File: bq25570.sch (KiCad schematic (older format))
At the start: 32 parts

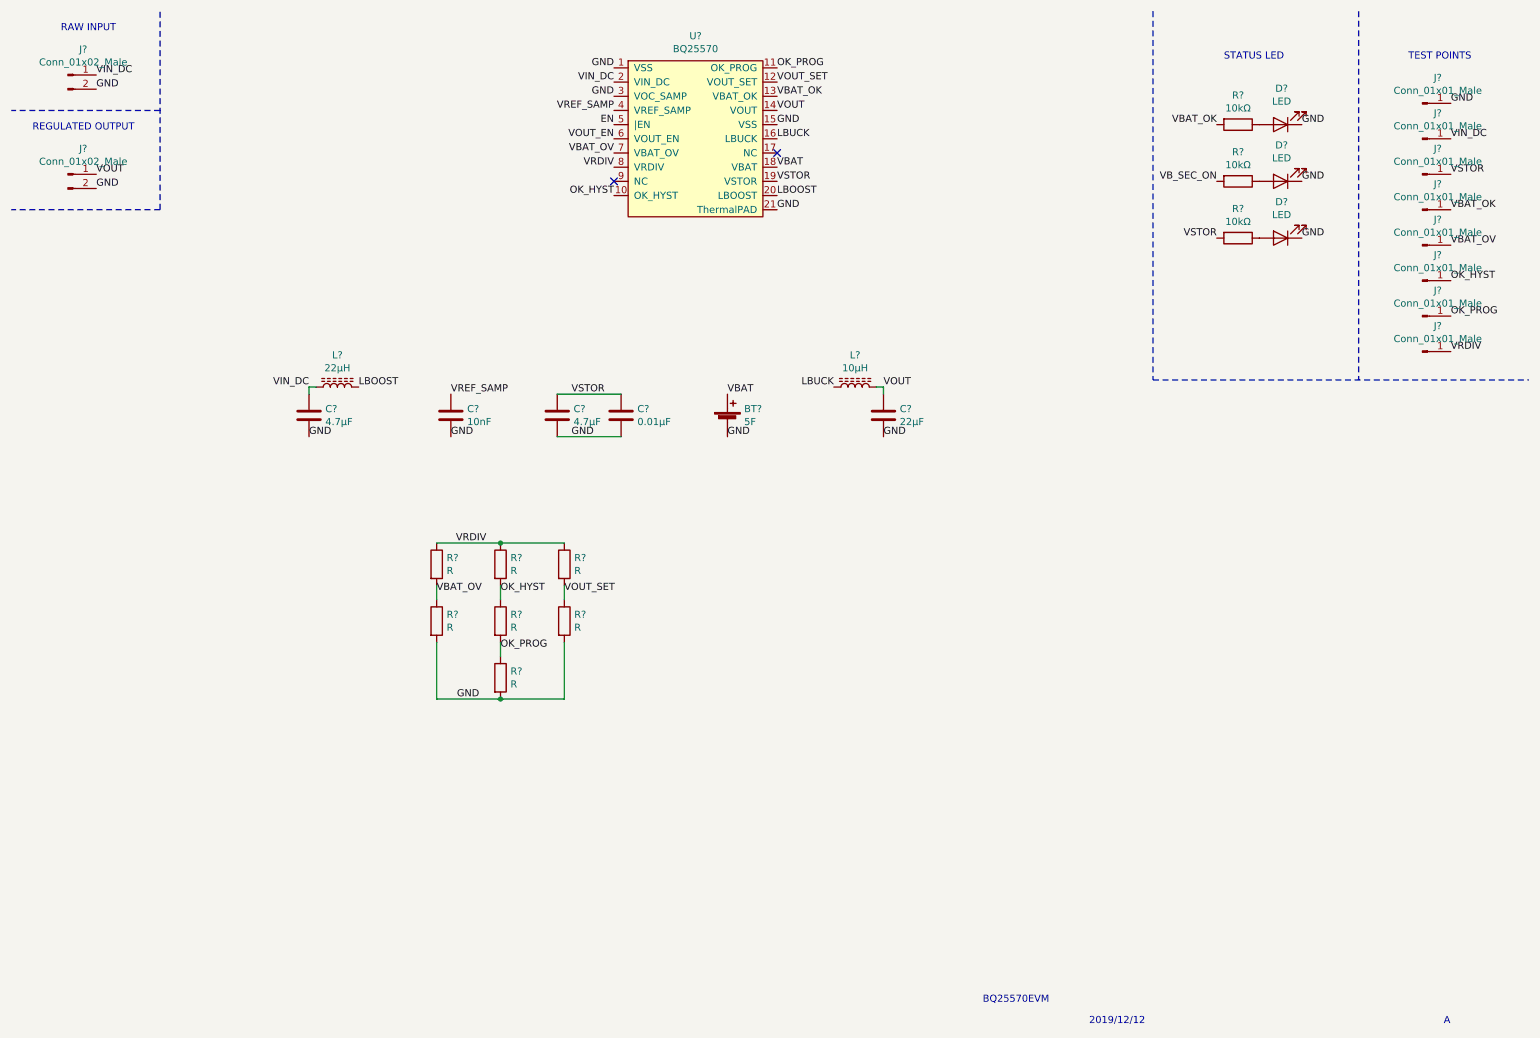
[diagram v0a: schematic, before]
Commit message: Schematic done
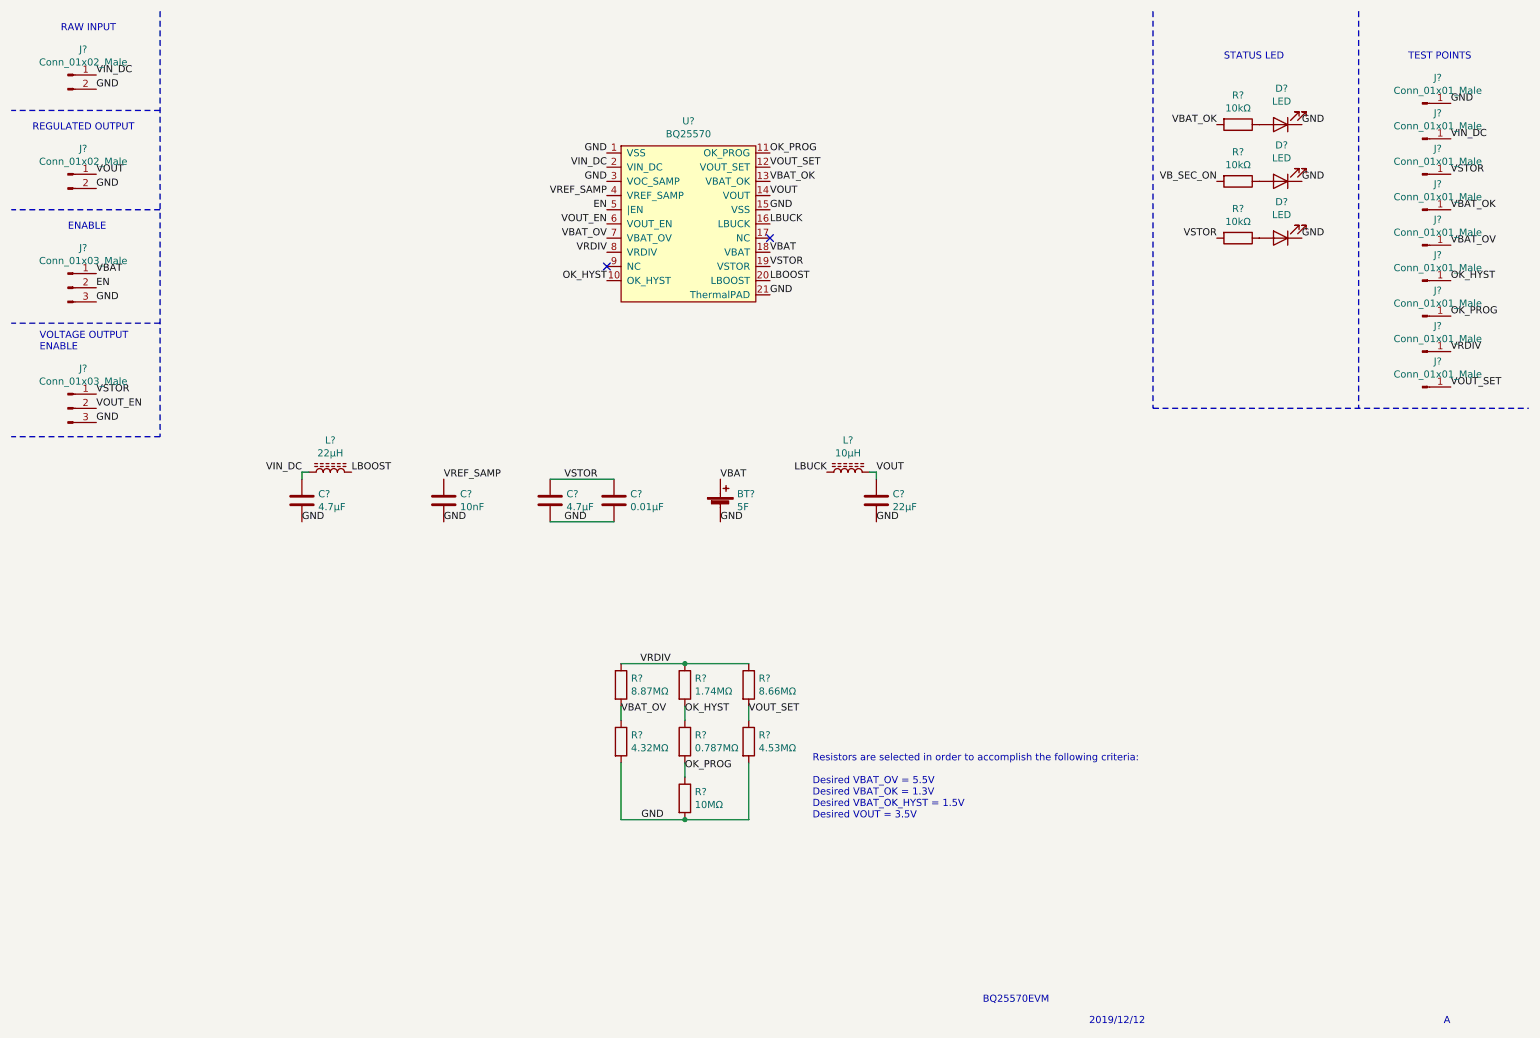
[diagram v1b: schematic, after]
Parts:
- added J?: Conn_01x01_Male, Connector_PinHeader_1.27mm:PinHeader_1x01_P1.27mm_Vertical, symbol Connector:Conn_01x01_Male
- added J? (x2): Conn_01x03_Male, Connector_PinHeader_1.27mm:PinHeader_1x03_P1.27mm_Vertical, symbol Connector:Conn_01x03_Male
- R?: value R -> 8.87MΩ
- R?: value R -> 4.32MΩ
- R?: value R -> 1.74MΩ
- R?: value R -> 0.787MΩ
- R?: value R -> 10MΩ
- R?: value R -> 8.66MΩ
- R?: value R -> 4.53MΩ
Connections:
- net EN: now also J?.2 (Pin_2)
- net GND: now also J?.3 (Pin_3), J?.3 (Pin_3)
- net VBAT: now also J?.1 (Pin_1)
- net VOUT_EN: now also J?.2 (Pin_2)
- net VOUT_SET: now also J?.1 (Pin_1)
- net VSTOR: now also J?.1 (Pin_1)
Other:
- note added: "ENABLE"
- note added: "Resistors are selected in order to accomplish the following criteria:\n\nDesired VBAT_OV = 5.5V\nDesired VBAT_OK = 1.3V\nDesired VBAT_OK_HYST = 1.5V\nDesired VOUT = 3.5V"
- note added: "VOLTAGE OUTPUT\nENABLE"
- moved on the sheet: BT?, C?, L?, R?, U?

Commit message: Schematic finished, components added, PCB design started
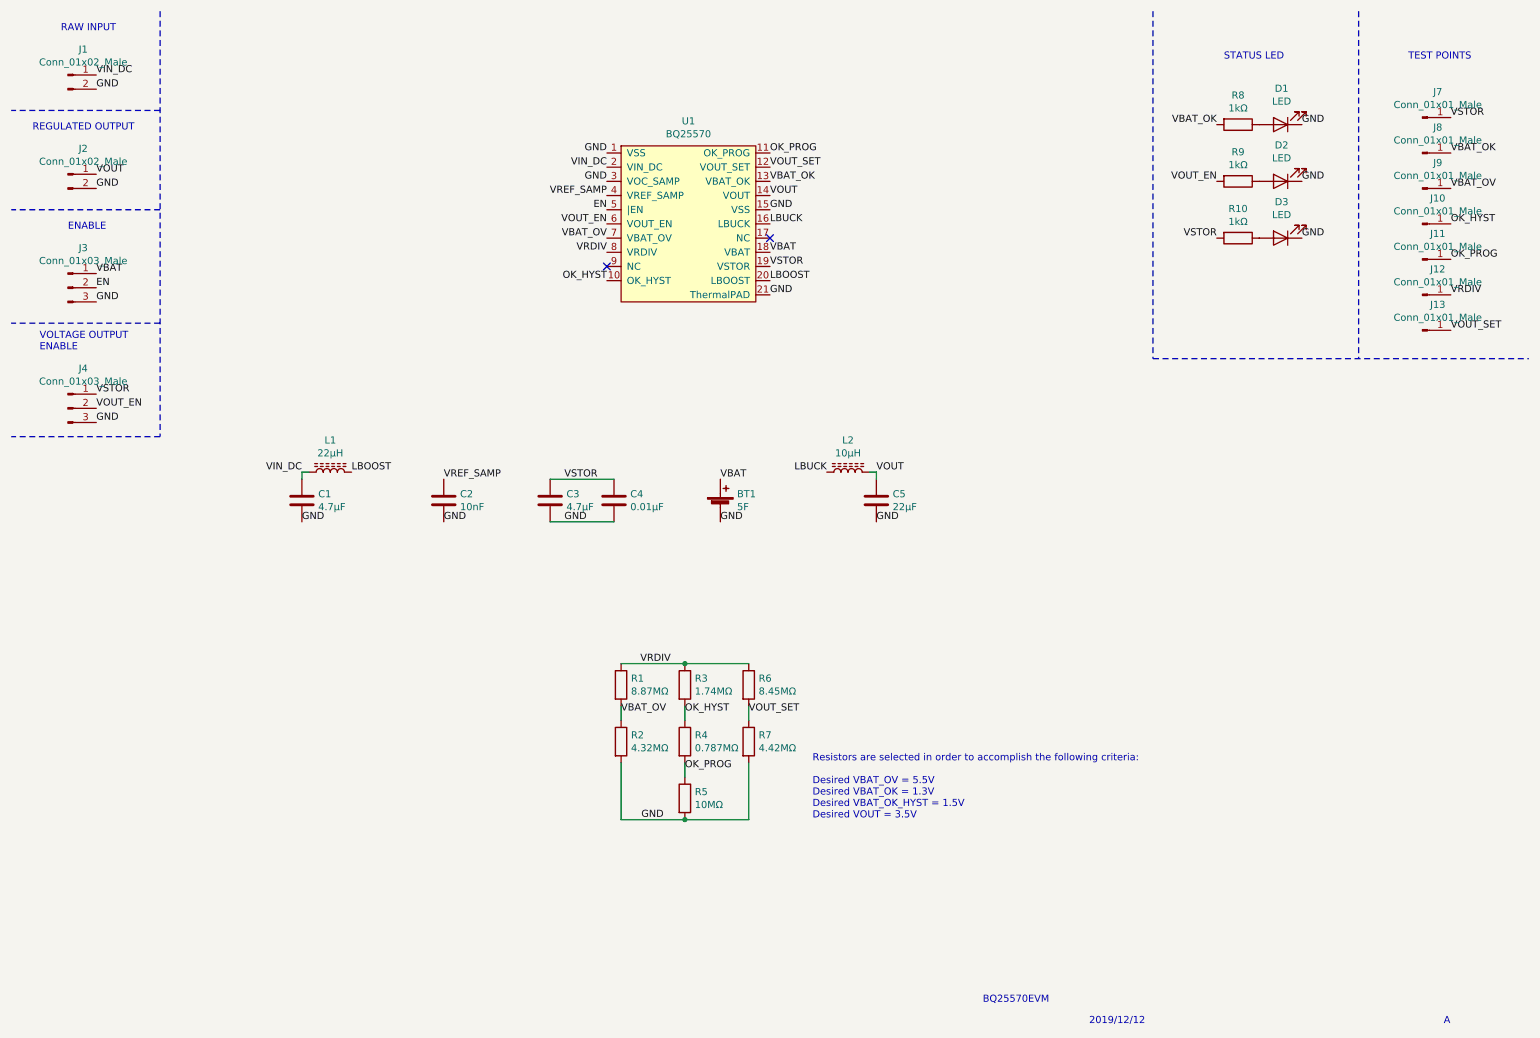
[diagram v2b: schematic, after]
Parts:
- removed J? (x2): Conn_01x01_Male, Connector_PinHeader_1.27mm:PinHeader_1x01_P1.27mm_Vertical, symbol Connector:Conn_01x01_Male
- BT1: renamed from BT?; footprint (none) -> Connector_PinHeader_2.00mm:PinHeader_1x02_P2.00mm_Vertical
- C1, C2, C3, C4, C5: renamed from C?; footprint (none) -> Capacitor_SMD:C_0805_2012Metric_Pad1.15x1.40mm_HandSolder
- J1, J2: renamed from J?; footprint Connector_PinHeader_1.27mm:PinHeader_1x02_P1.27mm_Vertical -> Connector_PinHeader_2.54mm:PinHeader_1x02_P2.54mm_Vertical
- J10, J11, J12, J13, J7, J8, J9: renamed from J?; footprint Connector_PinHeader_1.27mm:PinHeader_1x01_P1.27mm_Vertical -> Connector_PinHeader_2.54mm:PinHeader_1x01_P2.54mm_Vertical
- J3, J4: renamed from J?; footprint Connector_PinHeader_1.27mm:PinHeader_1x03_P1.27mm_Vertical -> Connector_PinHeader_2.54mm:PinHeader_1x03_P2.54mm_Vertical
- L1, L2: renamed from L?; footprint (none) -> Inductor_SMD:L_Coilcraft_LPS4018
- R1: renamed from R?; footprint (none) -> Resistor_SMD:R_0603_1608Metric_Pad1.05x0.95mm_HandSolder
- R10, R8, R9: renamed from R?; value 10kΩ -> 1kΩ
- R2, R3, R4, R5: renamed from R?; footprint (none) -> Resistor_SMD:R_0805_2012Metric_Pad1.15x1.40mm_HandSolder
- R6: renamed from R?; value 8.66MΩ -> 8.45MΩ; footprint (none) -> Resistor_SMD:R_0805_2012Metric_Pad1.15x1.40mm_HandSolder
- R7: renamed from R?; value 4.53MΩ -> 4.42MΩ; footprint (none) -> Resistor_SMD:R_0805_2012Metric_Pad1.15x1.40mm_HandSolder
- gave numbers to parts that had none: 4
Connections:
- net VB_SEC_ON is gone; now on net VOUT_EN: R9.2
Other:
- moved on the sheet: J10, J11, J12, J13, J7, J8, J9

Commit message: PCB layout done. Checking needed
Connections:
- net GND: now also U1.9 (NC)
- no-connect marks 2 -> 1
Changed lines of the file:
@@
 EESchema Schematic File Version 4
-LIBS:bq25570-cache
 EELAYER 30 0
 EELAYER END
@@
 	1    0    0    -1
 $EndComp
-NoConn ~ 4700 2300
 Text Notes 850  650  0    50   ~ 0
 RAW INPUT
@@
 Wire Notes Line
 	1550 500  1550 3500
+Text Label 4700 2300 2    50   ~ 0
+GND
 $EndSCHEMATC

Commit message: Footprint bt changed
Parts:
- BT1: footprint Connector_PinHeader_2.00mm:PinHeader_1x02_P2.00mm_Vertical -> Components:PinHeader_1x02_P5.50mm_Vertical
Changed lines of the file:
@@
 F 0 "BT1" H 5618 4096 50  0000 L CNN
 F 1 "5F" H 5618 4005 50  0000 L CNN
-F 2 "Connector_PinHeader_2.00mm:PinHeader_1x02_P2.00mm_Vertical" V 5500 4060 50  0001 C CNN
+F 2 "Components:PinHeader_1x02_P5.50mm_Vertical" V 5500 4060 50  0001 C CNN
 F 3 "http://www.farnell.com/datasheets/2579997.pdf" V 5500 4060 50  0001 C CNN
 	1    5500 4000

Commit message: BQ25570 footprint updated
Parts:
- U1: symbol BatteryManagement:BQ25570 -> bq25570-rescue:BQ25570-BatteryManagement
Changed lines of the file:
@@
 VRDIV
 $Comp
-L BatteryManagement:BQ25570 U1
+L bq25570-rescue:BQ25570-BatteryManagement U1
 U 1 1 5DF8A8E4
 P 5300 1950

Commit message: 0.01uF renamed to 10nF
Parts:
- C4: value 0.01μF -> 10nF
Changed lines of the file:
@@
 P 4750 3950
 F 0 "C4" H 4865 3996 50  0000 L CNN
-F 1 "0.01μF" H 4865 3905 50  0000 L CNN
+F 1 "10nF" H 4865 3905 50  0000 L CNN
 F 2 "Capacitor_SMD:C_0805_2012Metric_Pad1.15x1.40mm_HandSolder" H 4788 3800 50  0001 C CNN
 F 3 "~" H 4750 3950 50  0001 C CNN
